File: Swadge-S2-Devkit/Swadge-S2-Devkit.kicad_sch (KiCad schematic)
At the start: 100 parts, among them J1 CurrentMonitor, J10 LCD18, J11 LCD28, J2 DEBUG_BANK_C, J3 DEBUG_BANK_B, J4 DEBUG_BANK_A, J5 MICSEL, J6 TRYMIC, J7 LEDK_J, M1 VZ43FC1B5640007L, P1 USB_C_Plug_USB2.0, Q1 Q_N_FET, Q2 AP2003_PN_FET, Q3 AP2003_PN_FET, Q4 AP2003_PN_FET, SW1 4-1437565-2, SW13 touch-ring-6, SW14 SW_SPDT, SW2 4-1437565-2, SW3 4-1437565-2, SW4 4-1437565-2, SW5 4-1437565-2, SW6 4-1437565-2, SW7 4-1437565-2, SW8 4-1437565-2, SW9 4-1437565-2, U1 ESP32-S2-SOLO, U10 GENERIC_LDO_2.8, U11 LCD_240x240_1.3_12, U12 LCD_135x240_1.14_13, U15 LCD_240x240_1.54_12, U2 BUS_PCIexpress, U3 MT3410, U4 GS321-TR, U5 QMA7981, U6 INGHAi_GSPK2308P-8R0.5W, U9 GENERIC_LDO_1.8

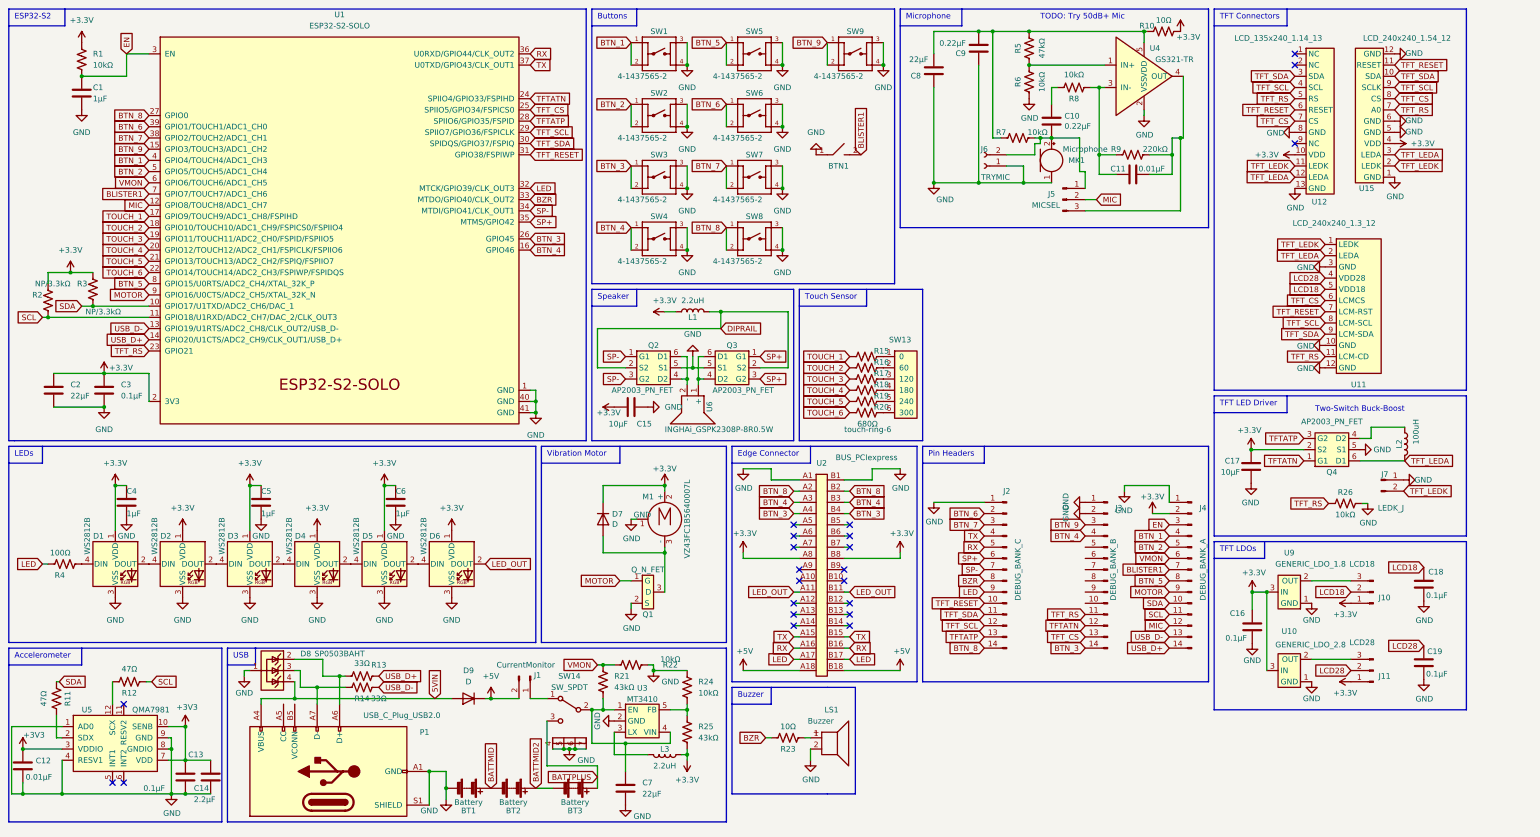
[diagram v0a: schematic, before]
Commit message: Fixed all import and DRC errors. Cleaned up BOM
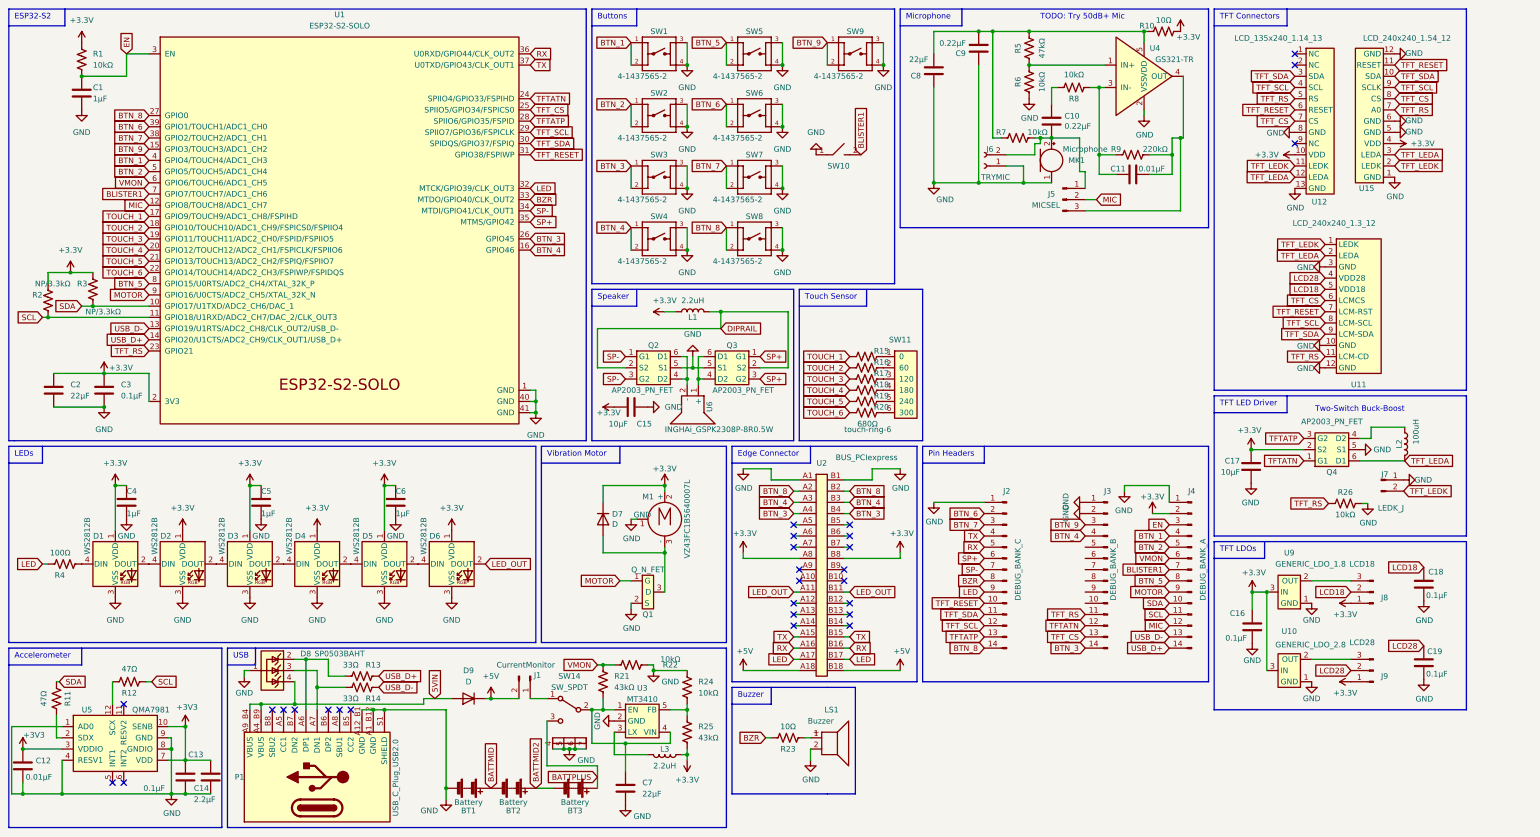
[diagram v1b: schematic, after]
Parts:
- C1, C10, C11, C12, C13, C14, C15, C16, C17, C18, C19, C2, C3, C4, C5, C6, C7, C8, C9, R1, R10, R11, R12, R13, R14, R15, R16, R17, R18, R19, R2, R20, R21, R22, R23, R24, R25, R26, R3, R4, R5, R6, R7, R8, R9: Digikey n/a -> (none)
- D7, D9: Substitutible Y -> (none)
- J2, J3: symbol Swadge_Parts:Conn_01x14_Male -> Swadge_Parts:Conn_02x07_Male; Cost100 (none) -> 25; Digikey (none) -> 2057-PH2-14-UA-ND
- J4: symbol Swadge_Parts:Conn_01x14_Male -> Swadge_Parts:Conn_02x07_Male; Cost100 45 -> 25; Digikey (none) -> 2057-PH2-14-UA-ND
- J6: symbol Connector:Conn_01x02_Female -> Swadge_Parts:Conn_01x02_Female; Cost100 (none) -> 90; Digikey (none) -> A26451-ND; Substitutable (none) -> Y
- L1, L3: LCSC C285966 -> C394950; Substitutable (none) -> Y
- L2: footprint Swadge_Parts:L_0805_2012Metric -> Swadge_Parts:L_1210_3225Metric; LCSC C88184 -> C1322422; Substitutable (none) -> Y
- LS1: Digikey LCSC Part #C219727 -> (none); LCSC (none) -> C219727
- P1: Digikey LCSC #C2765186 -> (none); LCSC (none) -> C2765186; Notes (none) -> https://www.usb.org/sites/default/files/documents/usb_type-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
- SW10: renamed from BTN1; Notes (none) -> DNP
- SW11: renamed from SW13; Notes (none) -> DNP; Substitutable Y -> (none)
- U10: Digikey LCSC# C347374 -> (none); LCSC (none) -> C347374
- U11: Digikey http://www.tftcolorlcddisplay.com/sale-11145258-thin-wearab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 -> (none); Notes (none) -> DNP
- U12: Digikey http://www.tftcolorlcddisplay.com/sale-11935168-smart-brace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 -> (none); Notes (none) -> DNP
- U15: Digikey http://www.tftcolorlcddisplay.com/sale-12419003-ips-240-240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 -> (none); Notes (none) -> DNP
- U3: Digikey LCSC Part #C883494 -> (none); LCSC (none) -> C883494
- U4: LCSC (none) -> C157695; Notes LCSC alternative: https://lcsc.com/product-detail/Low-Power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 -> (none)
- U5: Digikey LCSC Part #C457290 -> (none); LCSC (none) -> C457290; Notes Use https://lcsc.com/product-detail/Motion-Sensors-Accelero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 -> (none)
- U6: LCSC (none) -> C530532; Note LCSC #C530532 -> (none); Notes LCSC #C530532 -> (none)
- U9: Digikey LCSC# C347373 -> (none); LCSC (none) -> C347373
- renumbered J10 to J8, J11 to J9
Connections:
- net 5VIN: now also P1.A4_B9 (VBUS), P1.A9_B4 (VBUS); no longer P1.A4 (VBUS), P1.A9 (VBUS), P1.B4 (VBUS), P1.B9 (VBUS)
- net GND: now also P1.A12_B1 (GND), P1.A1_B12 (GND); no longer P1.A1 (GND), P1.A12 (GND), P1.B1 (GND), P1.B12 (GND)
- no-connect marks 22 -> 28

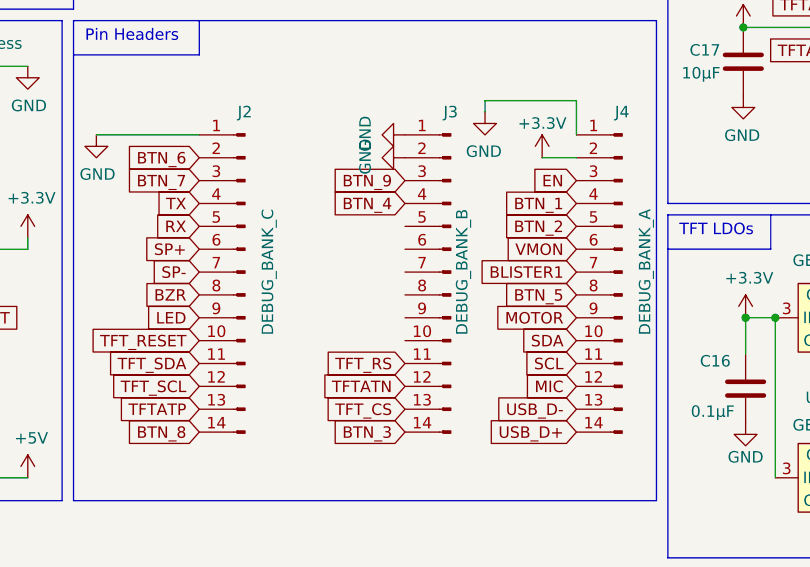
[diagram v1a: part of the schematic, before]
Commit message: Switch inductors, fix warnings
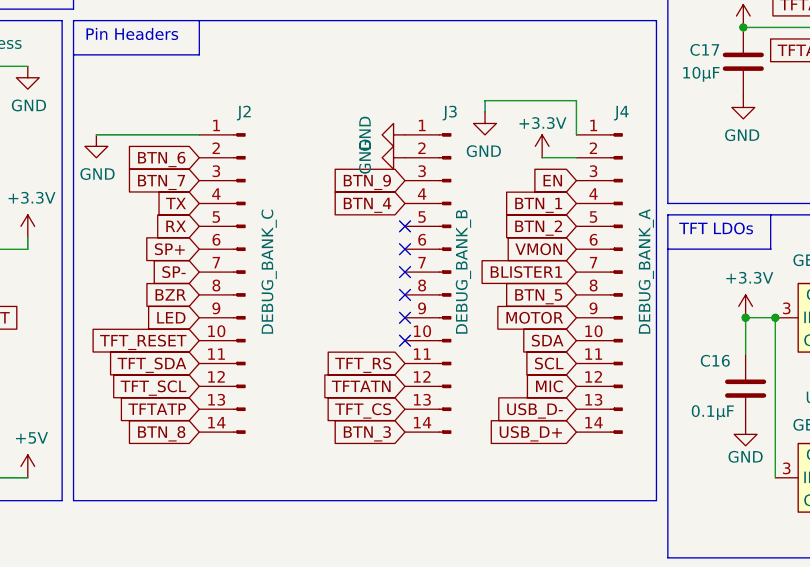
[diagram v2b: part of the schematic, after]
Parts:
- L1, L3: footprint Swadge_Parts:L_0603_1608Metric -> Swadge_Parts:L_1008_2520Metric; LCSC C394950 -> C216158
- L2: LCSC C1322422 -> C223229
- U1: Notes (none) -> Use module w. 4MB Flash, 2MB PSRAM (N4R2)
- U2: Notes (none) -> DNP
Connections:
- no-connect marks 28 -> 34

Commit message: Fixed warnings
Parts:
- C1, C10, C11, C12, C13, C14, C15, C16, C17, C18, C19, C2, C3, C4, C5, C6, C7, C8, C9, R1, R10, R11, R12, R13, R14, R15, R16, R17, R18, R19, R2, R20, R21, R22, R23, R24, R25, R26, R3, R4, R5, R6, R7, R8, R9: Notes 0603 Package -> (none)

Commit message: Update note for manufacturing Add silkscreen version Ignore output folder
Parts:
- J7, J8, J9: Notes (none) -> Put a jumper on this, similar to Digi-Key S9337-ND
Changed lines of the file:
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@@
       (effects (font (size 1.27 1.27)) hide)
     )
-    (property "Notes" "" (id 7) (at 321.818 162.56 0))
+    (property "Notes" "Put a jumper on this, similar to Digi-Key S9337-ND" (id 7) (at 321.818 162.56 0))
     (pin "1")
     (pin "2")
@@
       (effects (font (size 1.27 1.27)) hide)
     )
-    (property "Notes" "" (id 7) (at 326.136 120.65 0))
+    (property "Notes" "Put a jumper on this, similar to Digi-Key S9337-ND" (id 7) (at 326.136 120.65 0))
     (pin "1")
     (pin "2")
@@
       (effects (font (size 1.27 1.27)) hide)
     )
-    (property "Notes" "" (id 7) (at 321.818 144.78 0))
-    (pin "1")
-    (pin "2")
+    (property "Notes" "Put a jumper on this, similar to Digi-Key S9337-ND" (id 7) (at 321.818 144.78 0))
+    (pin "1")
+    (pin "2")

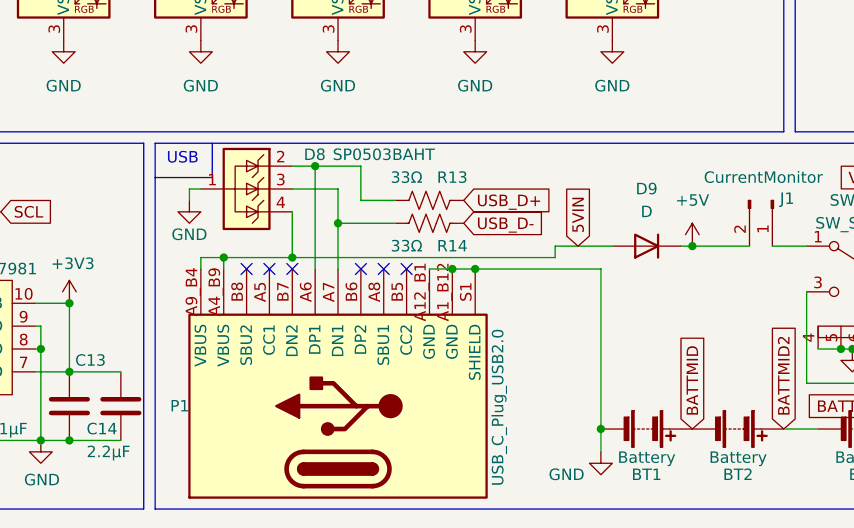
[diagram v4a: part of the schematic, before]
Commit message: Connect DP2 and DN2 on USB-C connector
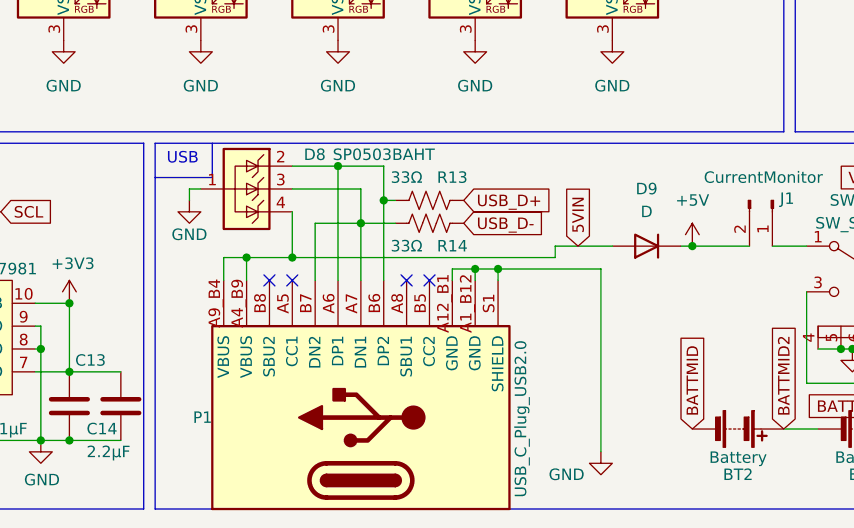
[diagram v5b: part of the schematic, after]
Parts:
- removed BT1: Battery, Swadge_Parts:2460, symbol Swadge_Parts:Battery
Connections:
- net at D8.2 (K), P1.A6 (DP1), R13.2: now also P1.B6 (DP2)
- net at D8.3 (K), P1.A7 (DN1), R14.2: now also P1.B7 (DN2)
- no-connect marks 34 -> 32
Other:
- moved on the sheet: P1

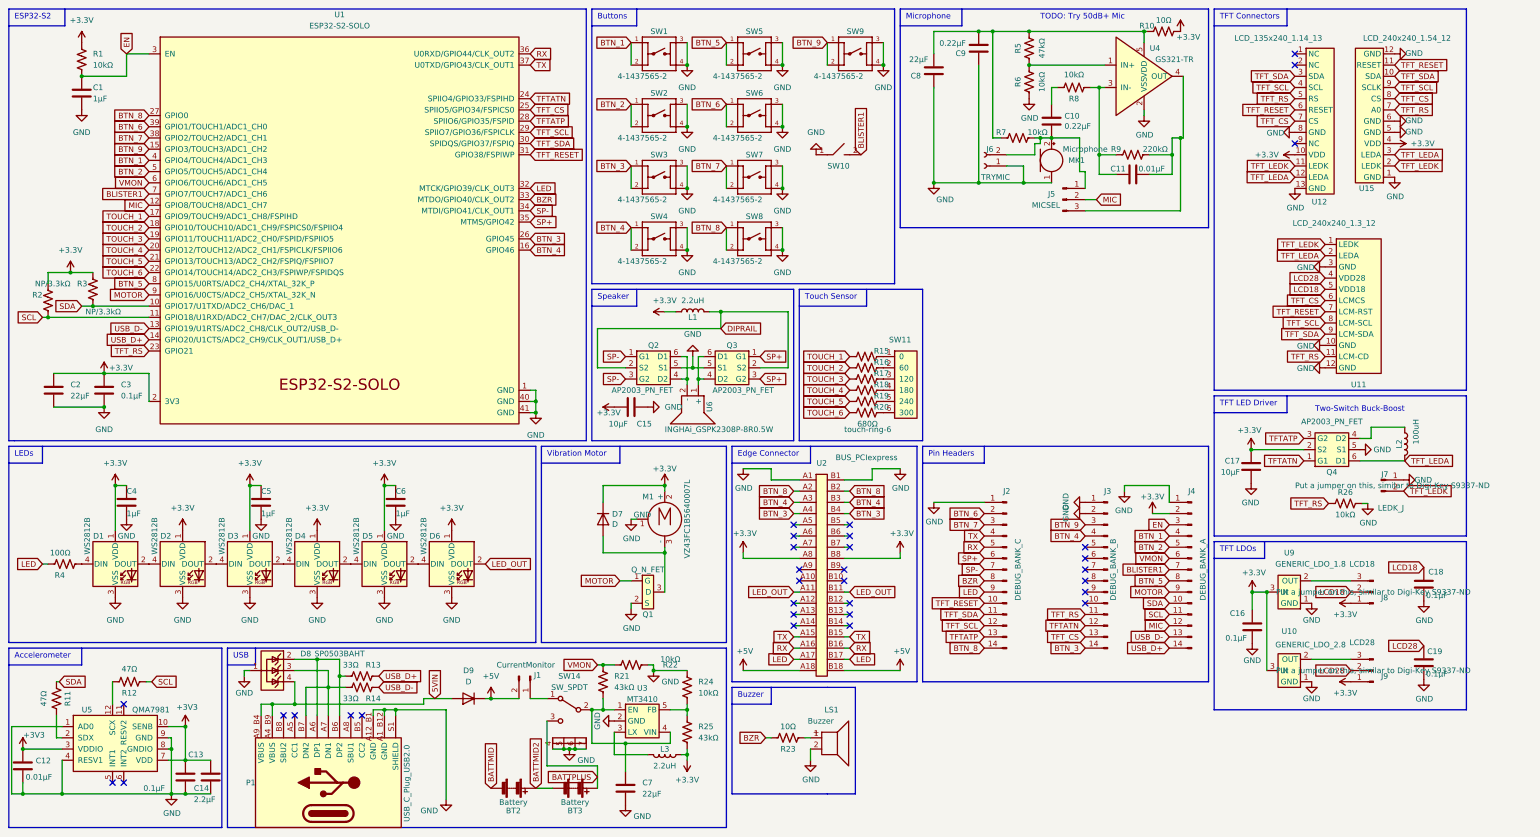
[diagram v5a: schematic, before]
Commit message: Remove accelerometer
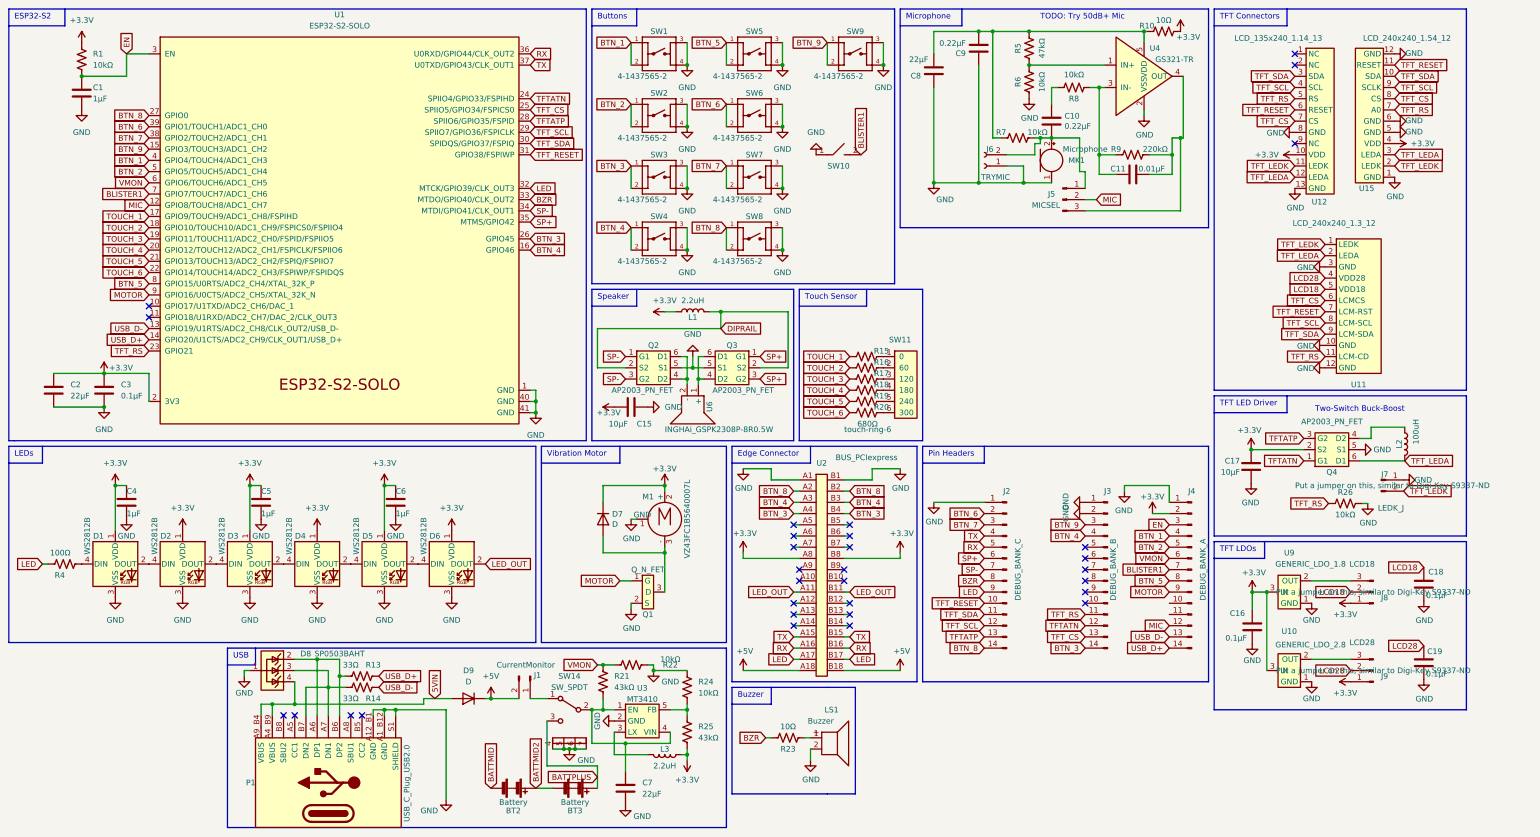
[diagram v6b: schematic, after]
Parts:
- removed C12: 0.01μF, Swadge_Parts:C_0603_1608Metric, symbol Swadge_Parts:C
- removed C13: 0.1μF, Swadge_Parts:C_0603_1608Metric, symbol Swadge_Parts:C
- removed C14: 2.2μF, Swadge_Parts:C_0603_1608Metric, symbol Swadge_Parts:C
- removed R11, R12: 47Ω, Swadge_Parts:R_0603_1608Metric, symbol Swadge_Parts:R_US
- removed R2, R3: NP/3.3kΩ, Swadge_Parts:R_0603_1608Metric, symbol Swadge_Parts:R_US
- removed U5: QMA7981, Swadge_Parts:QMA6981, symbol Swadge_Parts:QMA7981
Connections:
- net SCL: no longer names the net of U1.11 (GPIO18/U1RXD/ADC2_CH7/DAC_2/CLK_OUT3)
- net SCL: no longer J4.11 (Pin_11)
- net SDA: no longer names the net of U1.10 (GPIO17/U1TXD/ADC2_CH6/DAC_1)
- net SDA: no longer J4.10 (Pin_10)
- no-connect marks 32 -> 31
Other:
- note removed: "Accelerometer"
